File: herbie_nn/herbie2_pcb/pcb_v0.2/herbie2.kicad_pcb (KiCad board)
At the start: 2 copper layers, 119.4 x 96.5 mm, 95 parts, among them J1 GND, J10 CONN_04JST-PTH, J11 CONN_04JST-PTH, J12 Vin, J15 Conn_01x03_Male, J16 Conn_02x03_Odd_Even, J17 Conn_01x03, J18 Conn_01x02, J19 Conn_01x01, J2 5V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

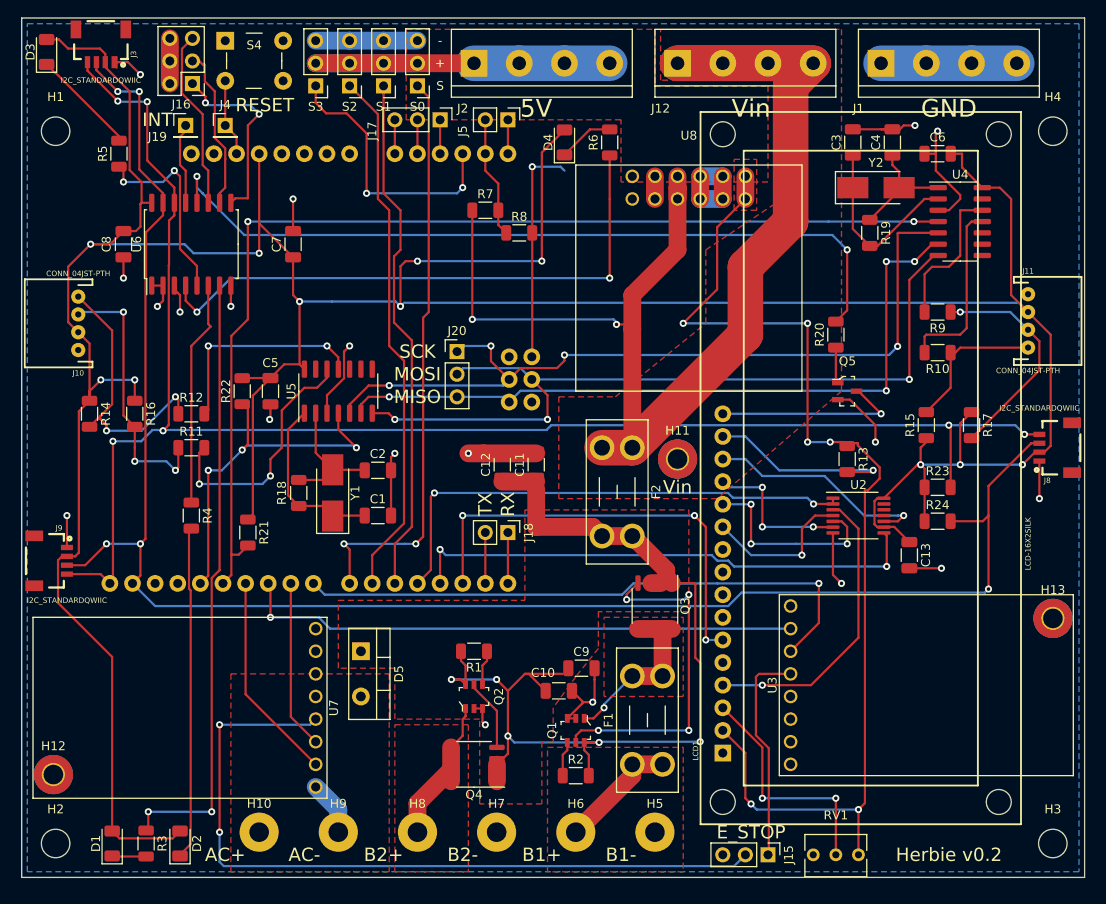
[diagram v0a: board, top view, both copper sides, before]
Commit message: started updating PCB for astromech support
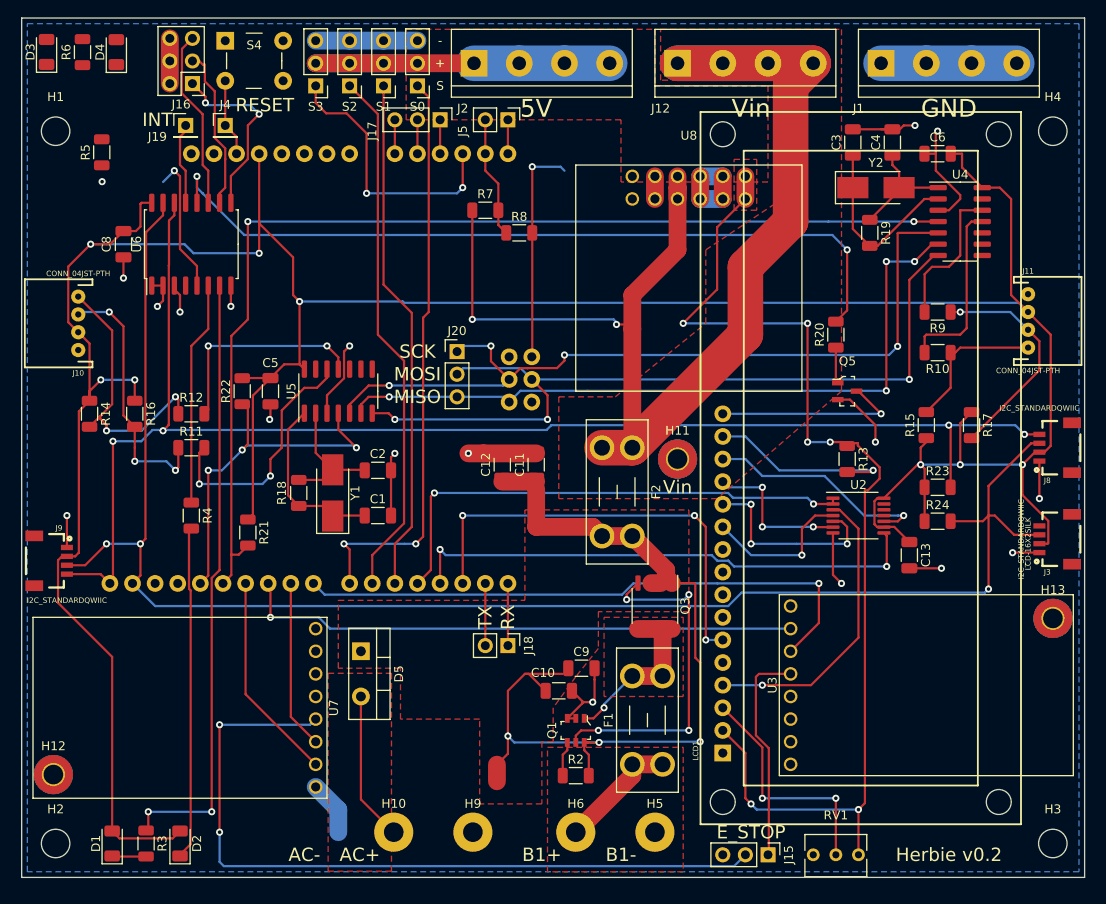
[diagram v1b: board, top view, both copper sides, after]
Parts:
- removed C7: .1uF, Capacitor_SMD:C_1206_3216Metric
- removed H7: GND_BATT2, MountingHole:MountingHole_2.2mm_M2_Pad
- removed H8: PWR_BATT2, MountingHole:MountingHole_2.2mm_M2_Pad
- removed Q2: LTC4412, digikey-footprints:SOT-23-6
- removed Q4: Si4427, js:SO-8_3.9x4.9mm_P1.27mm_Si4427
- removed R1: 470K, Resistor_SMD:R_1206_3216Metric
- moved J3 118.2 mm to (217.2, 97.9), turned to 90 degrees
- moved R6 60.1 mm to (109.7, 43.2)
- moved D4 51.3 mm to (113.5, 43.2)
- moved H10 15.1 mm to (144.7, 130.8)
- moved H9 15.1 mm to (153.5, 130.8)
- moved J18 12.7 mm to (157.5, 109.9)
- moved R5 1.94 mm to (111.9, 54.5)
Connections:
- net CLK_SERVO renamed SERVO2
- net DATA_SERVO renamed SERVO0
- net RCLK_SERVO renamed SERVO1
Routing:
- net Net-(R6-Pad1): track 65.2 -> 0.00 mm, vias 2 -> 0
- net 3.3V: track 403.0 -> 351.6 mm, vias 11 -> 8
- net SCL: track 181.1 -> 159.3 mm, vias 6 -> 4
- net BATT2: track 17.4 -> 0.00 mm
- net AC_PWR: track 0.00 -> 16.8 mm
- net SDA: track 195.9 -> 182.2 mm, vias 5 -> 3
- net VIN_FUSE: track 109.5 -> 96.8 mm, vias 5 -> 3
- net Net-(D3-Pad1): track 12.2 -> 0.00 mm
- net GND: track 177.6 -> 169.4 mm, vias 20 -> 18
- net Net-(Q2-Pad5): track 8.13 -> 0.00 mm
- net Net-(D4-Pad1): track 6.27 -> 0.00 mm
- net Net-(R5-Pad1): track 21.9 -> 15.8 mm
- net Net-(Q2-Pad4): track 3.94 -> 0.00 mm
- net Net-(B2-PadTX): track 5.72 -> 6.98 mm
- net Net-(B2-PadRX): track 5.72 -> 6.98 mm
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- removed copper zone on F.Cu, net BATT2
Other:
- board text removed: "B2+"
- board text removed: "B2-"

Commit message: added dome encoder
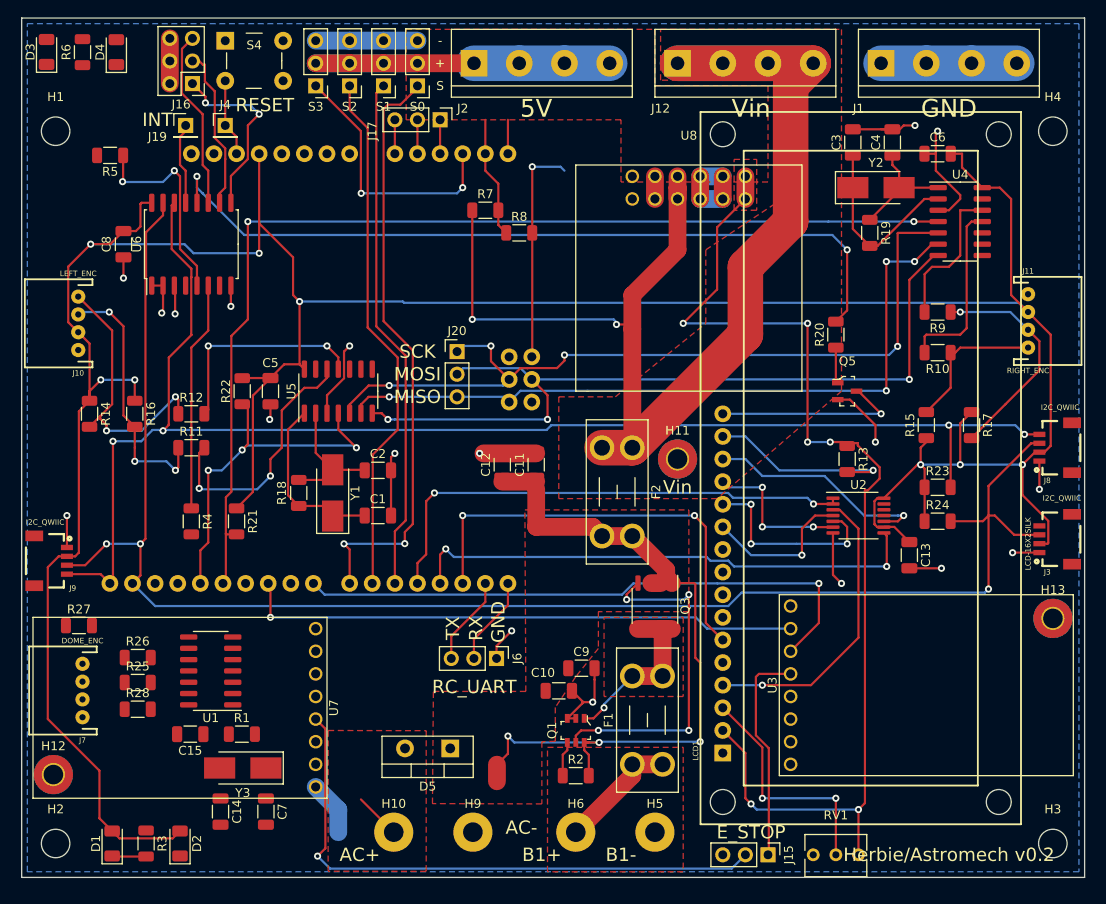
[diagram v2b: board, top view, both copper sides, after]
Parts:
- removed J18, J5: Conn_01x02, Connector_PinHeader_2.54mm:PinHeader_1x02_P2.54mm_Vertical
- added C14: 12pF, Capacitor_SMD:C_1206_3216Metric, F.Cu at (125.2, 128.5)
- added C15: .1uF, Capacitor_SMD:C_1206_3216Metric, F.Cu at (121.8, 119.8)
- added C7: 12pF, Capacitor_SMD:C_1206_3216Metric, F.Cu at (130.3, 128.5)
- added J6: RC_UART, Connector_PinHeader_2.54mm:PinHeader_1x03_P2.54mm_Vertical, F.Cu at (156.2, 111.3)
- added J7: DOME_ENC, Connectors:JST-4-PTH, F.Cu at (109.7, 114.9)
- added R1: 1M, Resistor_SMD:R_1206_3216Metric, F.Cu at (127.6, 119.8)
- added R25: 100, Resistor_SMD:R_1206_3216Metric, F.Cu at (115.9, 114.0)
- added R26: 100, Resistor_SMD:R_1206_3216Metric, F.Cu at (115.9, 111.2)
- added R27: 20K, Resistor_SMD:R_1206_3216Metric, F.Cu at (109.3, 107.6)
- added R28: 20K, Resistor_SMD:R_1206_3216Metric, F.Cu at (115.9, 117.0)
- added U1: LS7366R, Package_SO:SOIC-14_3.9x8.7mm_P1.27mm, F.Cu at (124.1, 112.7)
- added Y3: 20MHz, Crystal:Crystal_SMD_5032-2Pin_5.0x3.2mm_HandSoldering, F.Cu at (127.7, 123.6)
- J10: value CONN_04JST-PTH -> LEFT_ENC
- J11: value CONN_04JST-PTH -> RIGHT_ENC
- J3, J8, J9: value I2C_STANDARDQWIIC -> I2C_QWIIC
- moved D5 14.8 mm to (151.0, 121.4), turned to 180 degrees
- moved R21 1.79 mm to (127.0, 95.9)
- moved R5 1.00 mm to (112.8, 54.8), turned to 180 degrees
- moved R4 0.65 mm to (121.9, 95.9)
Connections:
- B2 pad A5: Net-(B2-PadA5) -> ENC3_SS
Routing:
- net Net-(R3-Pad1): track 68.8 -> 0.35 mm, vias 2 -> 0
- net Net-(D2-Pad1): track 37.5 -> 0.13 mm
- net MOTOR2_DIR: track 24.1 -> 0.54 mm
- net E_STOP2: track 86.2 -> 65.5 mm, vias 2 -> 1
- net MOTOR2_PWM: track 18.9 -> 0.00 mm
- net VIN_FUSE: track 96.8 -> 81.7 mm
- net AC_PWR: track 16.8 -> 5.21 mm
- net Net-(R5-Pad1): track 15.8 -> 23.3 mm
- net Net-(B2-PadA5): track 3.81 -> 0.00 mm
- net ENC3_SS: track 0.00 -> 3.81 mm
- net Net-(B2-PadTX): track 6.98 -> 10.0 mm
- net Net-(B2-PadRX): track 6.98 -> 10.0 mm
- net SCL: track 159.3 -> 161.4 mm
- net GND: track 169.4 -> 171.4 mm, vias 18 -> 19
- net SERVO0: track 65.3 -> 67.1 mm
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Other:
- board text added: "Herbie/Astromech v0.2"
- board text added: "RC_UART"
- board text removed: "Herbie v0.2"

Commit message: more PCB updates
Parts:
- removed J16: Conn_02x03_Odd_Even, Connector_PinHeader_2.54mm:PinHeader_2x03_P2.54mm_Vertical
- added J13: Conn_02x04_Odd_Even, Connector_PinHeader_2.54mm:PinHeader_2x04_P2.54mm_Vertical, F.Cu at (128.7, 41.9)
- added J14: AM_Right, Connector_PinHeader_2.54mm:PinHeader_1x02_P2.54mm_Vertical, F.Cu at (200.7, 107.7)
- added J5: Conn_01x03_Female, Connector_PinHeader_2.54mm:PinHeader_1x03_P2.54mm_Vertical, F.Cu at (120.0, 109.3)
- added JP1: SolderJumper_3_Open, Jumper:SolderJumper-3_P1.3mm_Open_RoundedPad1.0x1.5mm_NumberLabels, F.Cu at (156.9, 111.2)
- added Q2: 2N7002, digikey-footprints:SOT-23-3, F.Cu at (152.3, 113.0)
- added R29: 1K, Resistor_SMD:R_1206_3216Metric, F.Cu at (152.5, 109.4)
- added R30: 10K, Resistor_SMD:R_1206_3216Metric, F.Cu at (147.4, 109.4)
- J4: value Conn_01x01 -> AM_Left; footprint Connector_PinHeader_2.54mm:PinHeader_1x01_P2.54mm_Vertical -> Connector_PinHeader_2.54mm:PinHeader_1x02_P2.54mm_Vertical
- moved J4 81.6 mm to (133.0, 132.7), turned to 180 degrees
- moved J17 21.6 mm to (171.4, 52.4)
- moved J6 10.7 mm to (146.3, 115.3)
- moved S4 4.78 mm to (124.4, 46.5), turned to 180 degrees
- moved R28 4.30 mm to (116.0, 121.3), turned to 180 degrees
- moved R25 3.40 mm to (116.0, 117.4)
- moved U1 3.32 mm to (127.2, 113.9)
- moved Y3 2.47 mm to (129.0, 125.7)
- moved R26 2.40 mm to (116.0, 113.6)
- moved J19 2.25 mm to (119.4, 50.2)
- moved C7 2.08 mm to (129.1, 130.2)
- moved C15 1.98 mm to (123.1, 121.3)
- moved R1 1.78 mm to (128.7, 121.2)
- moved C14 1.71 mm to (125.0, 130.2)
- moved R7 1.57 mm to (156.5, 60.8)
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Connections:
- B2 pad RES: Net-(B2-PadRES) -> RESET
- B2 pad RX: Net-(B2-PadRX) -> SBUS_OUT
- J17 pad 3: Net-(B2-PadA0) -> GND
- J4 pad 1: Net-(B2-PadRES) -> GND
- J6 pad 2: Net-(B2-PadRX) -> SBUS_IN
- J6 pad 3: Net-(B2-PadTX) -> Net-(J6-Pad3)
- S4 pad 3: Net-(B2-PadRES) -> RESET
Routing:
- net 3.3V: track 352.6 -> 386.7 mm, vias 8 -> 10
- net Net-(R6-Pad1): track 0.00 -> 32.7 mm, vias 0 -> 2
- net Net-(B2-PadA1): track 3.81 -> 25.9 mm, vias 0 -> 1
- net Net-(B2-PadA2): track 3.81 -> 25.6 mm, vias 0 -> 1
- net RESET: track 0.00 -> 17.2 mm, vias 0 -> 2
- net Net-(D3-Pad1): track 0.00 -> 13.0 mm
- net Net-(B2-PadTX): track 10.0 -> 0.00 mm
- net Net-(B2-PadRX): track 10.0 -> 0.00 mm
- net Net-(B2-PadRES): track 8.72 -> 0.00 mm
- net DI1: track 18.3 -> 23.3 mm
- net Net-(D4-Pad1): track 0.00 -> 4.99 mm
- net GND: track 171.4 -> 166.5 mm
- net Net-(J19-Pad1): track 10.1 -> 6.05 mm
- net Net-(B2-PadA0): track 3.81 -> 0.00 mm
- net ENC3_SS: track 3.81 -> 0.00 mm
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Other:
- board text added: "5V_REG BOARD"
- board text added: "AM_Left"
- board text added: "AM_Right"
- board text added: "DNP"
- board text added: "SBUS"
- board text added: "UART1"
- board text added: "UART2"
- board text removed: "RESET"

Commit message: completed more routing
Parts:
- removed J19: Conn_01x01, Connector_PinHeader_2.54mm:PinHeader_1x01_P2.54mm_Vertical
- added JP2: SolderJumper_2_Open, Jumper:SolderJumper-2_P1.3mm_Open_RoundedPad1.0x1.5mm, F.Cu at (145.5, 58.5)
- moved C1 11.0 mm to (132.0, 97.0), turned to 270 degrees
- moved C2 9.55 mm to (136.2, 97.0), turned to 270 degrees
- moved C14 6.42 mm to (120.3, 125.8), turned to 180 degrees
- moved J14 6.32 mm to (195.1, 110.6), turned to 180 degrees
- moved R18 4.77 mm to (135.8, 88.3), turned to 180 degrees
- moved C7 3.15 mm to (126.1, 129.2), turned to 180 degrees
- moved R4 2.79 mm to (119.2, 95.3)
- moved R25 2.02 mm to (115.4, 119.3)
- moved R28 1.99 mm to (115.3, 123.2)
- moved R26 1.98 mm to (115.5, 115.5)
- moved Y1 1.49 mm to (136.4, 92.2), turned to 0 degrees
- moved Y3 1.20 mm to (127.8, 125.5)
- moved J5 1.15 mm to (120.0, 110.5)
- moved R29 0.95 mm to (152.8, 108.5)
- moved R30 0.90 mm to (147.4, 108.5)
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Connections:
- net SBUS_OUT renamed SBUS_IN_SEL
- B2 pad A0: Net-(B2-PadA0) -> A0
- B2 pad TX: Net-(B2-PadTX) -> SMART_PORT
- J5 pad 1: MOTOR1_DIR -> MOTOR2_DIR
- J5 pad 2: MOTOR2_DIR -> MOTOR1_DIR
- J6 pad 2: SBUS_IN -> SMART_PORT
- J6 pad 3: Net-(J6-Pad3) -> SBUS_IN
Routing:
- net ENC3_SS: track 0.00 -> 85.9 mm, vias 0 -> 2
- net Net-(R3-Pad1): track 0.35 -> 74.1 mm, vias 0 -> 2
- net 3.3V: track 386.7 -> 445.7 mm, vias 10 -> 14
- net MOTOR2_DIR: track 0.54 -> 54.1 mm, vias 0 -> 3
- net ENC_MISO: track 82.5 -> 132.9 mm, vias 4 -> 6
- net ENC_MOSI: track 92.4 -> 135.9 mm, vias 3 -> 5
- net ENC_SCK: track 92.2 -> 134.2 mm, vias 4 -> 6
- net Net-(D2-Pad1): track 0.13 -> 40.0 mm
- net MOTOR2_PWM: track 0.00 -> 30.1 mm
- net Net-(JP2-Pad2): track 6.05 -> 34.7 mm, vias 0 -> 2
- net SMART_PORT: track 0.00 -> 24.2 mm, vias 0 -> 1
- net SBUS_IN: track 0.00 -> 24.1 mm, vias 0 -> 1
- net Net-(JP1-Pad1): track 0.00 -> 18.6 mm, vias 0 -> 2
- net Net-(C7-Pad1): track 0.00 -> 16.0 mm
- net MOTOR1_DIR: track 63.4 -> 78.3 mm
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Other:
- board text added: "(INV)"
- board text added: "SBUS_IN"
- board text added: "SIG"
- board text removed: "INT"
- board text removed: "SBUS"

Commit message: updated pcb
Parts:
- removed H5: GND_BATT1, MountingHole:MountingHole_2.2mm_M2_Pad
- removed H9: GND_AC_PWR, MountingHole:MountingHole_2.2mm_M2_Pad
- added C16: .1uF, Capacitor_SMD:C_1206_3216Metric, F.Cu at (201.8, 106.5)
- added J16: Power, TerminalBlock:TerminalBlock_bornier-4_P5.08mm, F.Cu at (166.9, 131.0)
- added J18: SmartPort, Connector_PinHeader_2.54mm:PinHeader_1x02_P2.54mm_Vertical, F.Cu at (158.0, 108.7)
- added J19: Conn_01x04_Female, Connector_PinHeader_2.54mm:PinHeader_1x04_P2.54mm_Vertical, F.Cu at (214.2, 123.5)
- added J21: Conn_01x04_Female, Connector_PinHeader_2.54mm:PinHeader_1x04_P2.54mm_Vertical, F.Cu at (214.2, 106.5)
- added R31: 20K, Resistor_SMD:R_1206_3216Metric, F.Cu at (162.8, 59.6)
- added R32: 4.7K, Resistor_SMD:R_1206_3216Metric, F.Cu at (151.8, 116.2)
- added R33: 4.7K, Resistor_SMD:R_1206_3216Metric, F.Cu at (151.8, 118.7)
- added U9: TCA9534, Package_SO:SOIC-16W_7.5x10.3mm_P1.27mm, F.Cu at (209.2, 114.7)
- R30: value 10K -> 4.7K
- moved H6 8.45 mm to (173.6, 131.0)
- moved JP1 1.95 mm to (156.9, 113.2)
- moved JP2 1.70 mm to (147.2, 58.5)
- moved R29 1.65 mm to (151.2, 108.5)
- moved R2 1.41 mm to (165.1, 123.0)
- moved R30 1.13 mm to (146.3, 108.5)
- moved C10 0.83 mm to (164.0, 114.9)
- moved R27 0.68 mm to (108.6, 105.7)
- moved Q2 0.18 mm to (151.5, 112.8)
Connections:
- B2 pad VIN: Net-(B2-PadVIN) -> 5V_REG
- J6 pad 2: SMART_PORT -> 5V_REG
- JP1 pad 3: SBUS_IN -> SDIV
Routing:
- net 5V_REG: track 167.1 -> 251.4 mm, vias 6 -> 8
- net 3.3V: track 445.7 -> 482.4 mm, vias 14 -> 15
- net SCL: track 172.4 -> 192.4 mm
- net SMART_PORT: track 24.2 -> 6.04 mm, vias 1 -> 0
- net GND: track 178.6 -> 196.2 mm, vias 21 -> 23
- net Net-(J19-Pad1): track 0.00 -> 12.8 mm
- net Net-(J19-Pad4): track 0.00 -> 12.0 mm
- net BATT1: track 14.9 -> 4.67 mm
- net SDIV: track 0.00 -> 9.08 mm
- net Net-(J21-Pad4): track 0.00 -> 9.00 mm
- net Net-(J19-Pad3): track 0.00 -> 8.54 mm
- net AC_PWR: track 5.21 -> 0.00 mm
- net Net-(J19-Pad2): track 0.00 -> 4.99 mm
- net Net-(JP2-Pad2): track 34.7 -> 30.3 mm
- net Net-(J21-Pad3): track 0.00 -> 4.28 mm
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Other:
- rule trace_min: 0.2 -> 0.25
- board text added: "Astromech v0.2"
- board text added: "B+"
- board text added: "B-"
- board text added: "Herbie/"
- board text added: "I/O_INT"
- board text added: "RESET"
- board text added: "SP"
- board text removed: "B1+"
- board text removed: "B1-"
- board text removed: "Herbie/Astromech v0.2"

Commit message: updated PCB
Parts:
- added ARDUINO_PWR1: SolderJumper_3_Open, Jumper:SolderJumper-3_P1.3mm_Open_RoundedPad1.0x1.5mm_NumberLabels, F.Cu at (136.4, 60.7)
- added R34: 20K, Resistor_SMD:R_1206_3216Metric, F.Cu at (118.6, 54.4)
- moved R20 1.52 mm to (195.8, 74.9)
- moved Q5 1.05 mm to (196.6, 81.0)
- renumbered D1 to LED1, D2 to LED2, D3 to LED3, D4 to LED4
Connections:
- B2 pad VIN: 5V_REG -> ARD_VIN
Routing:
- net ARD_VIN: track 0.00 -> 7.46 mm
- net 3.3V: track 482.4 -> 489.0 mm
- net Net-(JP2-Pad2): track 30.3 -> 33.6 mm
- net E_STOP1: track 25.6 -> 22.4 mm
- net Net-(LCD1-Pad3): track 26.6 -> 23.9 mm
- net GND: track 196.2 -> 194.4 mm
- net 5V_REG: track 251.4 -> 250.5 mm, vias 8 -> 6
- net LCD_RS: track 35.8 -> 35.1 mm, vias 1 -> 0
- net Net-(R6-Pad1): track 32.7 -> 33.4 mm
- net ENC_SCK: track 132.5 -> 131.9 mm
- net BATT1_F: vias 1 -> 0
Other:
- board text added: "5V_REG"
- board text added: "NC"

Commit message: updated pcb
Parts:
- added J22: Conn_01x01, Connector_PinHeader_2.00mm:PinHeader_1x01_P2.00mm_Vertical, F.Cu at (218.4, 114.0)
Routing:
- net Net-(J22-Pad1): track 0.00 -> 15.1 mm
